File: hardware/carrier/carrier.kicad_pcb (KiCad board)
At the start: 2 copper layers, 80 x 60 mm, 4 parts

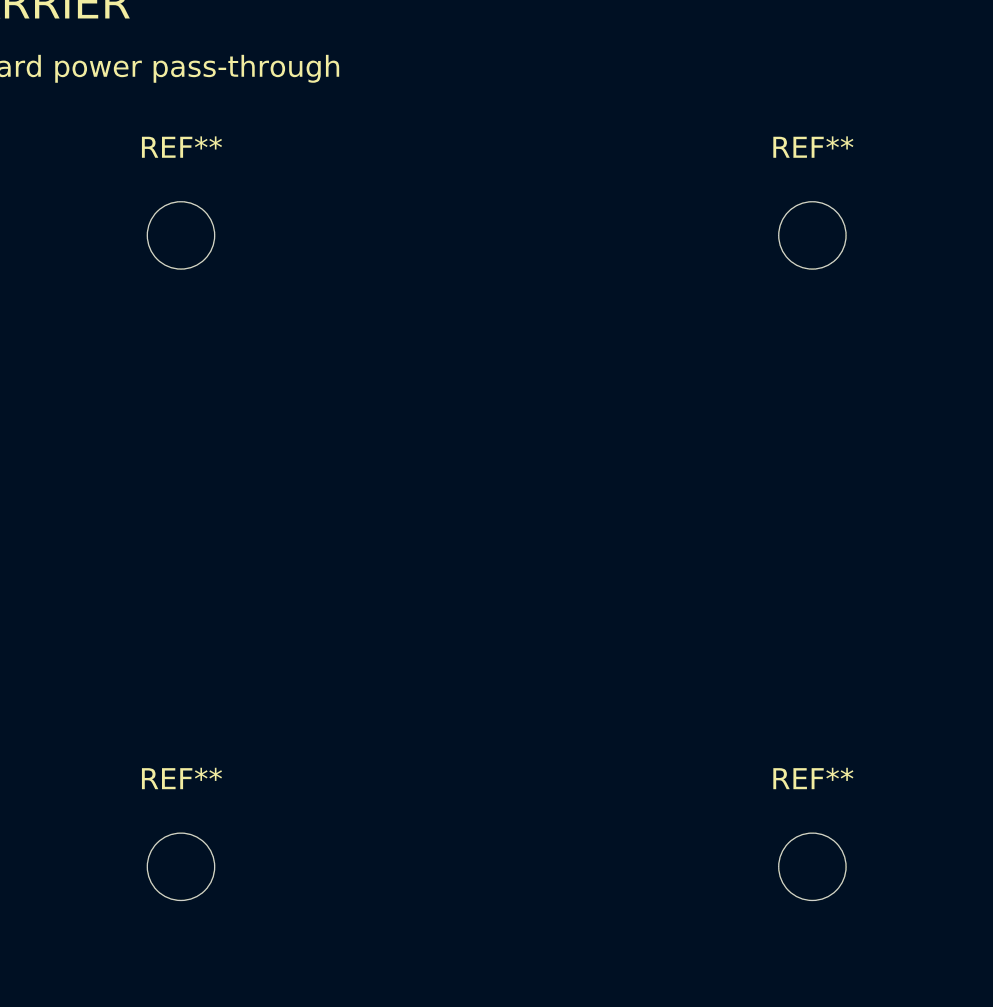
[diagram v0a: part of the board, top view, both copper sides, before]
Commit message: Complete the 3-board TMR system: real board instances, verified independent
The three FMU sheets were placeholders. They are now three instances of the
real 492-symbol board, and the array's defining property - three boards that
fail independently but share one voting bus - is demonstrable from KiCad's
netlist rather than asserted.

The blocker was that KiCad's Eagle import wires every cross-page net as a
global label: 136 distinct, 123 spanning pages, no internal hierarchy.
Global means global to the whole project, so instantiating that design three
times would have shorted all 120 non-shared nets together across FMU-A/B/C -
every SPI bus, every MCU pin, every internal rail - while looking completely
normal on screen.

gen_fmu_hierarchical.py generates hardware/fmu-v2/ from the pristine import,
which stays untouched and re-importable: 120 multi-page nets become
hierarchical labels plus sheet pins on a new container root, joined there by
local labels, so connectivity survives but is scoped to one instance; 12
single-page nets become local labels; CAN_H/CAN_L/GND/SAFETY stay global,
which is correct, since those four are what the modules genuinely share.

That is heavy automated surgery on a design nobody can eyeball, so
check_fmu_conversion.py exports a netlist from the pristine import and from
the converted copy and compares them net by net: 262 multi-pin nets on both
sides, joining exactly the same pins.

annotate_tmr_instances.py then gives each instance its own designators
(C101 -> C101A/B/C) by writing one (path ...) entry per instance, the
mechanism KiCad's own test project uses for a thrice-instantiated subsheet.
It derives the hierarchy prefix from the files rather than assuming it -
KiCad 10 roots symbol paths at the root document's uuid, KiCad 7 did not, and
the imported pages use a third form. Assuming any one of them silently gave
all three boards the "A" reference.

Verified on the full system netlist:
  885 component instances, 885 distinct references,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
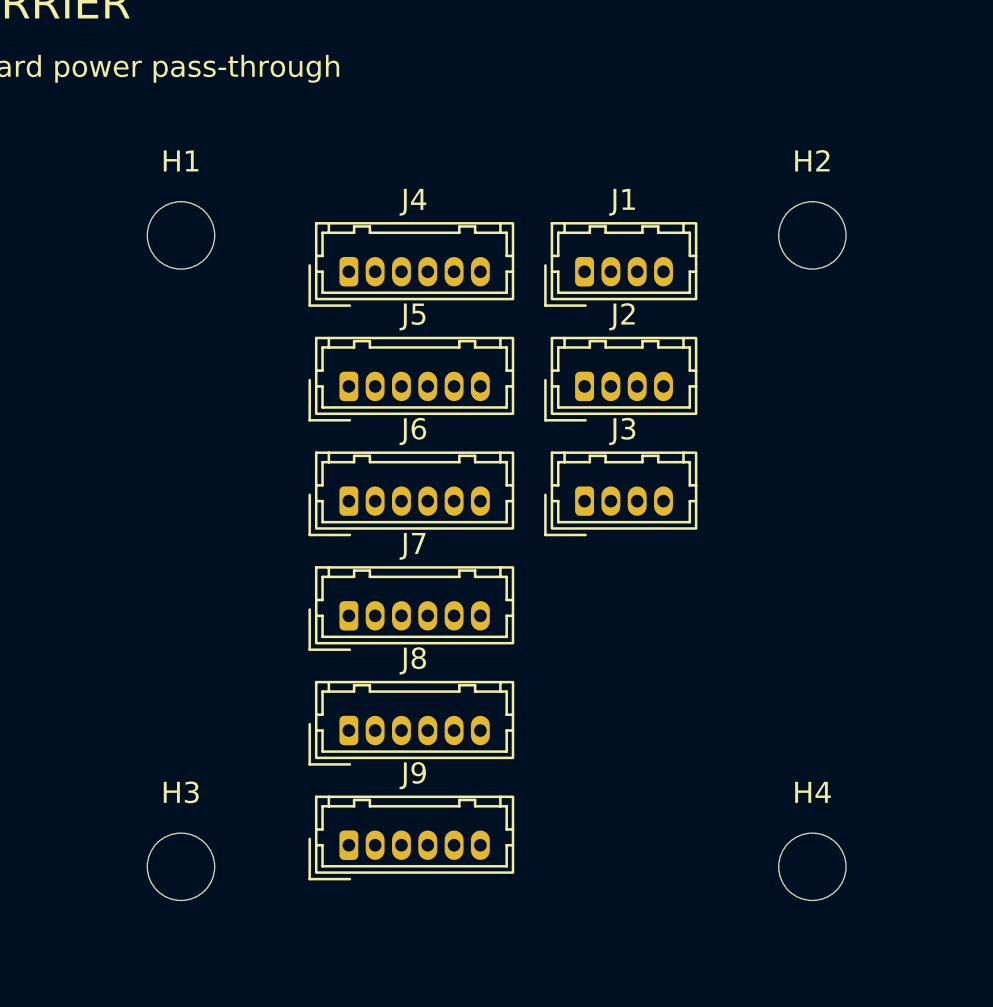
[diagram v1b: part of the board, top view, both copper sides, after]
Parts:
- added J1: CAN A -> module J405, Connector_Hirose:Hirose_DF13-04P-1.25DSA_1x04_P1.25mm_Vertical, F.Cu at (144.2, 116.7)
- added J2: CAN B -> module J405, Connector_Hirose:Hirose_DF13-04P-1.25DSA_1x04_P1.25mm_Vertical, F.Cu at (144.2, 122.2)
- added J3: CAN C -> module J405, Connector_Hirose:Hirose_DF13-04P-1.25DSA_1x04_P1.25mm_Vertical, F.Cu at (144.2, 127.6)
- added J4: BRICK A in, Connector_Hirose:Hirose_DF13-06P-1.25DSA_1x06_P1.25mm_Vertical, F.Cu at (133.0, 116.7)
- added J5: BRICK B in, Connector_Hirose:Hirose_DF13-06P-1.25DSA_1x06_P1.25mm_Vertical, F.Cu at (133.0, 122.2)
- added J6: BRICK C in, Connector_Hirose:Hirose_DF13-06P-1.25DSA_1x06_P1.25mm_Vertical, F.Cu at (133.0, 127.6)
- added J7: PWR A -> module J601, Connector_Hirose:Hirose_DF13-06P-1.25DSA_1x06_P1.25mm_Vertical, F.Cu at (133.0, 133.1)
- added J8: PWR B -> module J601, Connector_Hirose:Hirose_DF13-06P-1.25DSA_1x06_P1.25mm_Vertical, F.Cu at (133.0, 138.5)
- added J9: PWR C -> module J601, Connector_Hirose:Hirose_DF13-06P-1.25DSA_1x06_P1.25mm_Vertical, F.Cu at (133.0, 144.0)
- renumbered REF** to H1, REF** to H2, REF** to H3, REF** to H4

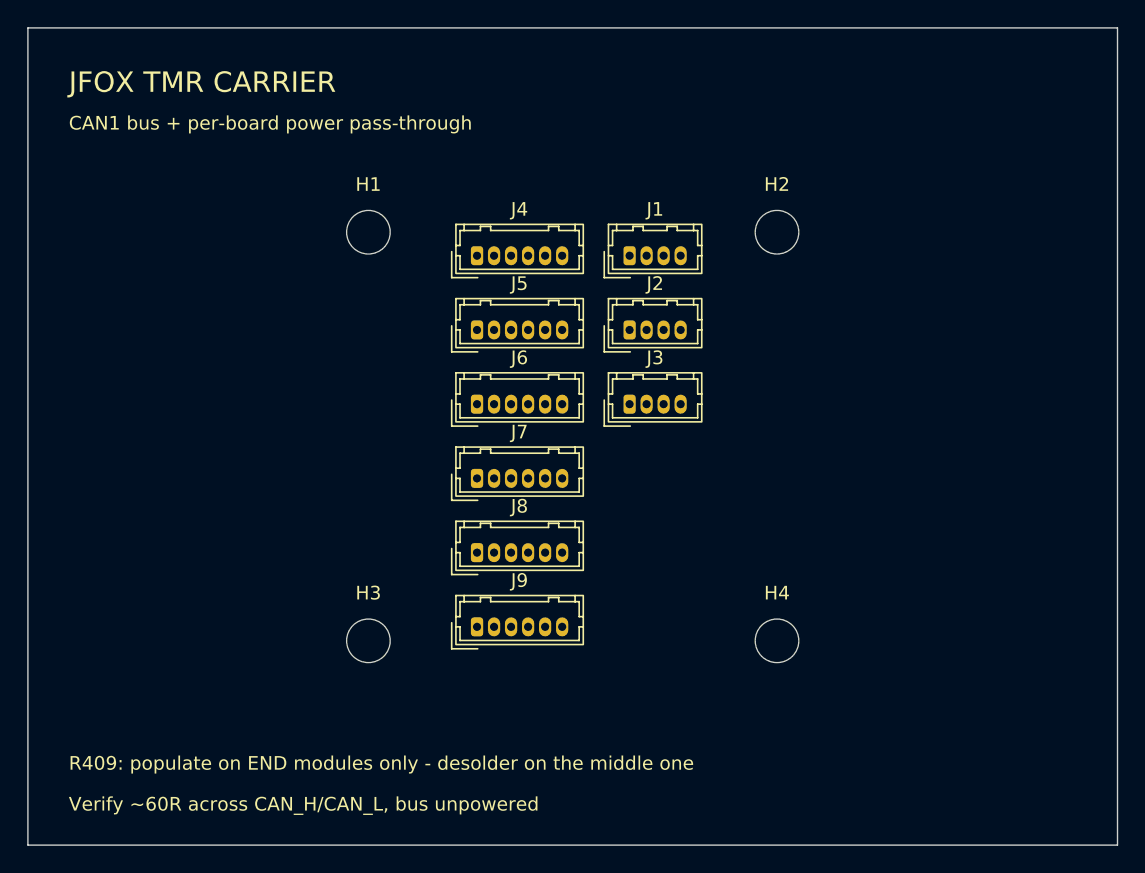
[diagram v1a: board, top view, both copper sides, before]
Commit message: Place and route the carrier board: DRC clean, fabrication set exports
F8 loaded the netlist onto the board, which left the nine connectors in a
heap on top of the mounting holes with no copper. route_carrier.py places
them and lays the routing. DRC: 0 violations, 0 unconnected.

The layout is arranged so the routing is trivially correct rather than
merely DRC-clean. The three CAN connectors sit in a column at the same x, so
their pin 2s line up and CAN_H is one straight trace down the board with
CAN_L parallel 1.25mm away - a real daisy chain, no stubs, and the pair
stays tight. No termination is placed; each module carries a fixed 120R
R409, and the silkscreen says which one to desolder.

Power runs left to right, brick in on one column and out to the module on
another at matching pin positions. Routed straight across at pin height the
three signals per board would collide, so each drops to the back layer at
its own offset and comes back up: three parallel runs, no crossings, and no
copper shared between boards - the independence the netlist asserts is now
also true of the copper.

Ground is routed explicitly rather than left to the pours. A zone that fails
to fill conducts nothing while still looking poured on screen, so the board
is made correct by copper and the two planes are a bonus. It runs as three
vertical trunks joined by one horizontal link at y=133; a horizontal at pin
height would cross the power stubs leaving the module-side connectors, and
one at row+3 would land inside an M3 keepout.

Two zone details cost a cycle each and are recorded so they do not again:
KiCad 10 names the net ((net "GND")) where KiCad 7 used an index plus
net_name, and the fill must be enabled explicitly with (fill yes ...).
Either one wrong and DRC reports all 15 ground pads unconnected.

The silkscreen also had to move - gen_carrier_pcb.py writes the board title
before placement is known, and it landed on J1.

Full fabrication set exports: 24 files - gerbers, drill, job file, p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
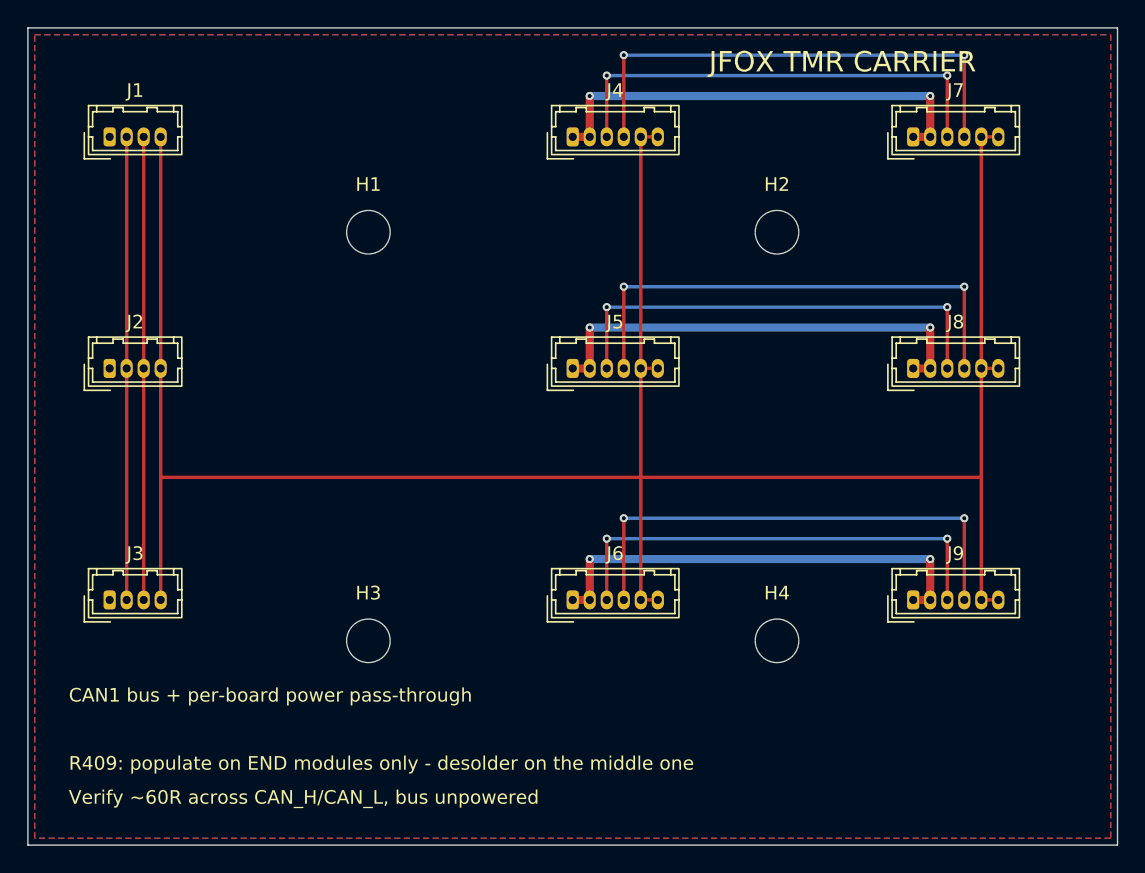
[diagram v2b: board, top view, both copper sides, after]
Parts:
- moved J3 40.8 mm to (106.0, 142.0)
- moved J7 40.7 mm to (165.0, 108.0)
- moved J1 39.2 mm to (106.0, 108.0)
- moved J2 38.3 mm to (106.0, 125.0)
- moved J8 34.8 mm to (165.0, 125.0)
- moved J9 32.1 mm to (165.0, 142.0)
- moved J6 16.0 mm to (140.0, 142.0)
- moved J4 11.2 mm to (140.0, 108.0)
- moved J5 7.57 mm to (140.0, 125.0)
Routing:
- net GND: track 0.00 -> 169.8 mm
- net /BATT_V_C: track 0.00 -> 37.0 mm, vias 0 -> 2
- net /BATT_V_B: track 0.00 -> 37.0 mm, vias 0 -> 2
- net /BATT_V_A: track 0.00 -> 37.0 mm, vias 0 -> 2
- net CAN_L: track 0.00 -> 34.0 mm
- net CAN_H: track 0.00 -> 34.0 mm
- net /BATT_I_C: track 0.00 -> 34.0 mm, vias 0 -> 2
- net /BATT_I_B: track 0.00 -> 34.0 mm, vias 0 -> 2
- net /BATT_I_A: track 0.00 -> 34.0 mm, vias 0 -> 2
- net /VBRICK_C: track 0.00 -> 33.5 mm, vias 0 -> 2
- net /VBRICK_B: track 0.00 -> 33.5 mm, vias 0 -> 2
- net /VBRICK_A: track 0.00 -> 33.5 mm, vias 0 -> 2
- added copper zone on B.Cu, net GND
- added copper zone on F.Cu, net GND
